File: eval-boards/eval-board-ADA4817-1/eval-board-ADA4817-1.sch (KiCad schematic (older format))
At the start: 27 parts, among them J2 -VIN, J3 +VIN, J4 Conn_01x03_Male, J5 VOUT, U1 ADA4817-1

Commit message: second-order_active_filter
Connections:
- net GNDREF: now also C10.1; no longer C10.2
- net VEE: now also C10.2; no longer C10.1
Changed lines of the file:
@@
 EESchema Schematic File Version 4
+LIBS:eval-board-ADA4817-1-cache
 EELAYER 29 0
 EELAYER END
@@
 F 3 "~" H 7400 4950 50  0001 C CNN
 	1    7400 4950
-	1    0    0    -1
-$EndComp
-$Comp
+	-1   0    0    1
+$EndComp
+$Comp

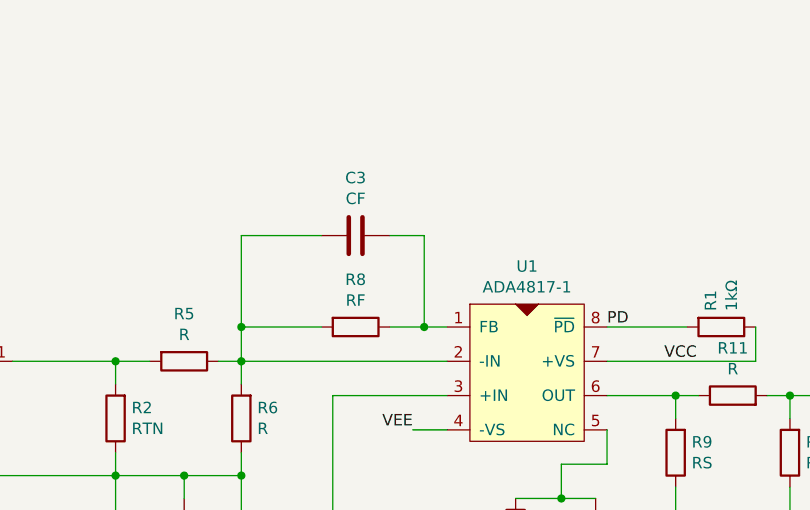
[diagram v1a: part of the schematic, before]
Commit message: power_and_RF_updated
修正了ADA4817和有源滤波器的电源线管脚、反馈电阻和焊盘handsold
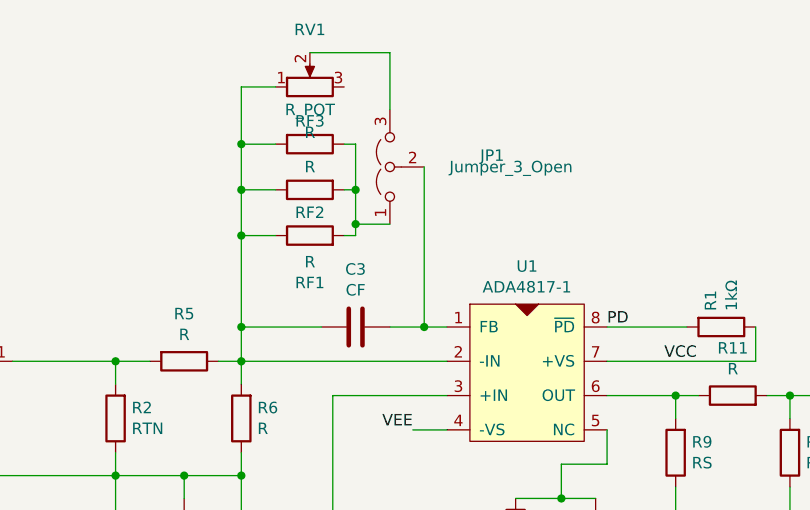
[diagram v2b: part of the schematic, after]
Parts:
- added JP1: Jumper_3_Open, Jumper:SolderJumper-3_P1.3mm_Open_RoundedPad1.0x1.5mm_NumberLabels, symbol Jumper:Jumper_3_Open
- added RF2, RF3: R, Resistor_SMD:R_0603_1608Metric_Pad1.05x0.95mm_HandSolder, symbol Device:R
- added RV1: R_POT, Connector_PinSocket_2.54mm:PinSocket_1x03_P2.54mm_Vertical, symbol Device:R_POT
- C1, C2, C3, C5, C6, C7, C8, C9: footprint Capacitor_SMD:C_0603_1608Metric -> Capacitor_SMD:C_0603_1608Metric_Pad1.05x0.95mm_HandSolder
- C10, C4: footprint Capacitor_SMD:CP_Elec_4x5.3 -> Capacitor_SMD:CP_Elec_4x5.4
- J4: footprint Connector_PinSocket_2.54mm:PinSocket_1x03_P2.54mm_Vertical -> Connector_JST:JST_XH_B3B-XH-A_1x03_P2.50mm_Vertical
- R1, R10, R11, R12, R2, R3, R4, R5, R6, R7, R9: footprint Resistor_SMD:R_0603_1608Metric -> Resistor_SMD:R_0603_1608Metric_Pad1.05x0.95mm_HandSolder
- RF1: renamed from R8; value RF -> R; footprint Resistor_SMD:R_0603_1608Metric -> Resistor_SMD:R_0603_1608Metric_Pad1.05x0.95mm_HandSolder
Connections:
- net at C3.1, U1.1 (FB): now also JP1.2 (C); no longer RF1.1
- net at C3.2, R5.1, R6.2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: now also RF1.1, RF2.1, RF3.2, RV1.1; no longer RF1.2
- new net: JP1.1 (A), RF1.2, RF2.2, RF3.1
- new net: JP1.3 (B), RV1.2
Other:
- moved on the sheet: C3, RF1
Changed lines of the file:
@@
 F 0 "R5" V 3843 2800 50  0000 C CNN
 F 1 "R" V 3934 2800 50  0000 C CNN
-F 2 "Resistor_SMD:R_0603_1608Metric" V 3980 2800 50  0001 C CNN
+F 2 "Resistor_SMD:R_0603_1608Metric_Pad1.05x0.95mm_HandSolder" V 3980 2800 50  0001 C CNN
 F 3 "~" H 4050 2800 50  0001 C CNN
 	1    4050 2800
@@
 F 0 "R6" H 4230 3004 50  0000 R CNN
 F 1 "R" H 4230 3095 50  0000 R CNN
-F 2 "Resistor_SMD:R_0603_1608Metric" V 4230 3050 50  0001 C CNN
+F 2 "Resistor_SMD:R_0603_1608Metric_Pad1.05x0.95mm_HandSolder" V 4230 3050 50  0001 C CNN
 F 3 "~" H 4300 3050 50  0001 C CNN
 	1    4300 3050
@@
 F 0 "R2" H 3680 3004 50  0000 R CNN
 F 1 "RTN" H 3680 3095 50  0000 R CNN
-F 2 "Resistor_SMD:R_0603_1608Metric" V 3680 3050 50  0001 C CNN
+F 2 "Resistor_SMD:R_0603_1608Metric_Pad1.05x0.95mm_HandSolder" V 3680 3050 50  0001 C CNN
 F 3 "~" H 3750 3050 50  0001 C CNN
 	1    3750 3050
@@
 	3100 3000 3100 3300
 Connection ~ 3750 3300
-$Comp
-L Device:R R8
-U 1 1 5D1F3FF1
+Wire Wire Line
+	4650 2650 4300 2650
+Wire Wire Line
+	4300 2650 4300 2800
+$Comp
+L Device:C C3
+U 1 1 5D1F4AF7
 P 4800 2650
-F 0 "R8" V 4593 2650 50  0000 C CNN
-F 1 "RF" V 4684 2650 50  0000 C CNN
-F 2 "Resistor_SMD:R_0603_1608Metric" V 4730 2650 50  0001 C CNN
+F 0 "C3" V 4548 2650 50  0000 C CNN
+F 1 "CF" V 4639 2650 50  0000 C CNN
+F 2 "Capacitor_SMD:C_0603_1608Metric_Pad1.05x0.95mm_HandSolder" H 4838 2500 50  0001 C CNN
 F 3 "~" H 4800 2650 50  0001 C CNN
 	1    4800 2650
@@
 $EndComp
 Wire Wire Line
-	4950 2650 5100 2650
-Wire Wire Line
-	4650 2650 4300 2650
-Wire Wire Line
-	4300 2650 4300 2800
-$Comp
-L Device:C C3
-U 1 1 5D1F4AF7
-P 4800 2250
-F 0 "C3" V 4548 2250 50  0000 C CNN
-F 1 "CF" V 4639 2250 50  0000 C CNN
-F 2 "Capacitor_SMD:C_0603_1608Metric" H 4838 2100 50  0001 C CNN
-F 3 "~" H 4800 2250 50  0001 C CNN
-	1    4800 2250
-	0    1    1    0
-$EndComp
-Wire Wire Line
-	4650 2250 4300 2250
-Wire Wire Line
 	4300 2250 4300 2650
 Connection ~ 4300 2650
-Wire Wire Line
-	4950 2250 5100 2250
-Wire Wire Line
-	5100 2250 5100 2650
-Connection ~ 5100 2650
-Wire Wire Line
-	5100 2650 5200 2650
 $Comp
 L Device:R R4
@@
 F 0 "R4" V 3793 4100 50  0000 C CNN
 F 1 "R" V 3884 4100 50  0000 C CNN
-F 2 "Resistor_SMD:R_0603_1608Metric" V 3930 4100 50  0001 C CNN
+F 2 "Resistor_SMD:R_0603_1608Metric_Pad1.05x0.95mm_HandSolder" V 3930 4100 50  0001 C CNN
 F 3 "~" H 4000 4100 50  0001 C CNN
 	1    4000 4100
@@
 F 0 "R3" H 3680 3754 50  0000 R CNN
 F 1 "RTP" H 3680 3845 50  0000 R CNN
-F 2 "Resistor_SMD:R_0603_1608Metric" V 3680 3800 50  0001 C CNN
+F 2 "Resistor_SMD:R_0603_1608Metric_Pad1.05x0.95mm_HandSolder" V 3680 3800 50  0001 C CNN
 F 3 "~" H 3750 3800 50  0001 C CNN
 	1    3750 3800
@@
 F 0 "R7" H 4230 3754 50  0000 R CNN
 F 1 "R" H 4230 3845 50  0000 R CNN
-F 2 "Resistor_SMD:R_0603_1608Metric" V 4230 3800 50  0001 C CNN
+F 2 "Resistor_SMD:R_0603_1608Metric_Pad1.05x0.95mm_HandSolder" V 4230 3800 50  0001 C CNN
 F 3 "~" H 4300 3800 50  0001 C CNN
 	1    4300 3800
@@
 F 0 "R9" H 6130 3154 50  0000 R CNN
 F 1 "RS" H 6130 3245 50  0000 R CNN
-F 2 "Resistor_SMD:R_0603_1608Metric" V 6130 3200 50  0001 C CNN
+F 2 "Resistor_SMD:R_0603_1608Metric_Pad1.05x0.95mm_HandSolder" V 6130 3200 50  0001 C CNN
 F 3 "~" H 6200 3200 50  0001 C CNN
 	1    6200 3200
@@
 F 0 "R11" V 6657 2950 50  0000 C CNN
 F 1 "R" V 6566 2950 50  0000 C CNN
-F 2 "Resistor_SMD:R_0603_1608Metric" V 6380 2950 50  0001 C CNN
+F 2 "Resistor_SMD:R_0603_1608Metric_Pad1.05x0.95mm_HandSolder" V 6380 2950 50  0001 C CNN
 F 3 "~" H 6450 2950 50  0001 C CNN
 	1    6450 2950
@@
 F 0 "R12" H 6630 3154 50  0000 R CNN
 F 1 "R" H 6630 3245 50  0000 R CNN
-F 2 "Resistor_SMD:R_0603_1608Metric" V 6630 3200 50  0001 C CNN
+F 2 "Resistor_SMD:R_0603_1608Metric_Pad1.05x0.95mm_HandSolder" V 6630 3200 50  0001 C CNN
 F 3 "~" H 6700 3200 50  0001 C CNN
 	1    6700 3200
@@
 F 0 "C5" H 6315 3696 50  0000 L CNN
 F 1 "CL" H 6315 3605 50  0000 L CNN
-F 2 "Capacitor_SMD:C_0603_1608Metric" H 6238 3500 50  0001 C CNN
+F 2 "Capacitor_SMD:C_0603_1608Metric_Pad1.05x0.95mm_HandSolder" H 6238 3500 50  0001 C CNN
 F 3 "~" H 6200 3650 50  0001 C CNN
 	1    6200 3650
@@
 F 0 "R10" V 5707 3550 50  0000 C CNN
 F 1 "R" V 5616 3550 50  0000 C CNN
-F 2 "Resistor_SMD:R_0603_1608Metric" V 5430 3550 50  0001 C CNN
+F 2 "Resistor_SMD:R_0603_1608Metric_Pad1.05x0.95mm_HandSolder" V 5430 3550 50  0001 C CNN
 F 3 "~" H 5500 3550 50  0001 C CNN
 	1    5500 3550
@@
 F 0 "C6" V 5598 3550 50  0000 C CNN
 F 1 "C" V 5689 3550 50  0000 C CNN
-F 2 "Capacitor_SMD:C_0603_1608Metric" H 5888 3400 50  0001 C CNN
+F 2 "Capacitor_SMD:C_0603_1608Metric_Pad1.05x0.95mm_HandSolder" H 5888 3400 50  0001 C CNN
 F 3 "~" H 5850 3550 50  0001 C CNN
 	1    5850 3550
@@
 F 0 "C8" V 5448 4000 50  0000 C CNN
 F 1 "C" V 5539 4000 50  0000 C CNN
-F 2 "Capacitor_SMD:C_0603_1608Metric" H 5738 3850 50  0001 C CNN
+F 2 "Capacitor_SMD:C_0603_1608Metric_Pad1.05x0.95mm_HandSolder" H 5738 3850 50  0001 C CNN
 F 3 "~" H 5700 4000 50  0001 C CNN
 	1    5700 4000
@@
 F 0 "R1" H 6330 2604 50  0000 R CNN
 F 1 "1kΩ" H 6330 2695 50  0000 R CNN
-F 2 "Resistor_SMD:R_0603_1608Metric" V 6330 2650 50  0001 C CNN
+F 2 "Resistor_SMD:R_0603_1608Metric_Pad1.05x0.95mm_HandSolder" V 6330 2650 50  0001 C CNN
 F 3 "~" H 6400 2650 50  0001 C CNN
 	1    6400 2650
@@
 F 0 "C10" H 7515 4996 50  0000 L CNN
 F 1 "10uF" H 7515 4905 50  0000 L CNN
-F 2 "Capacitor_SMD:CP_Elec_4x5.3" H 7400 4950 50  0001 C CNN
+F 2 "Capacitor_SMD:CP_Elec_4x5.4" H 7400 4950 50  0001 C CNN
 F 3 "~" H 7400 4950 50  0001 C CNN
 	1    7400 4950
@@
 F 0 "C4" H 4915 4946 50  0000 L CNN
 F 1 "10uF" H 4915 4855 50  0000 L CNN
-F 2 "Capacitor_SMD:CP_Elec_4x5.3" H 4800 4900 50  0001 C CNN
+F 2 "Capacitor_SMD:CP_Elec_4x5.4" H 4800 4900 50  0001 C CNN
 F 3 "~" H 4800 4900 50  0001 C CNN
 	1    4800 4900
@@
 F 0 "C1" H 4315 4946 50  0000 L CNN
 F 1 "0.1uF" H 4315 4855 50  0000 L CNN
-F 2 "Capacitor_SMD:C_0603_1608Metric" H 4238 4750 50  0001 C CNN
+F 2 "Capacitor_SMD:C_0603_1608Metric_Pad1.05x0.95mm_HandSolder" H 4238 4750 50  0001 C CNN
 F 3 "~" H 4200 4900 50  0001 C CNN
 	1    4200 4900
@@
 F 0 "C9" H 7215 4996 50  0000 L CNN
 F 1 "0.1uF" H 7215 4905 50  0000 L CNN
-F 2 "Capacitor_SMD:C_0603_1608Metric" H 7138 4800 50  0001 C CNN
+F 2 "Capacitor_SMD:C_0603_1608Metric_Pad1.05x0.95mm_HandSolder" H 7138 4800 50  0001 C CNN
 F 3 "~" H 7100 4950 50  0001 C CNN
 	1    7100 4950
@@
 F 0 "C7" H 6815 4996 50  0000 L CNN
 F 1 "0.1uF" H 6815 4905 50  0000 L CNN
-F 2 "Capacitor_SMD:C_0603_1608Metric" H 6738 4800 50  0001 C CNN
+F 2 "Capacitor_SMD:C_0603_1608Metric_Pad1.05x0.95mm_HandSolder" H 6738 4800 50  0001 C CNN
 F 3 "~" H 6700 4950 50  0001 C CNN
 	1    6700 4950
@@
 F 0 "C2" H 4665 4946 50  0000 L CNN
 F 1 "0.1uF" H 4665 4855 50  0000 L CNN
-F 2 "Capacitor_SMD:C_0603_1608Metric" H 4588 4750 50  0001 C CNN
+F 2 "Capacitor_SMD:C_0603_1608Metric_Pad1.05x0.95mm_HandSolder" H 4588 4750 50  0001 C CNN
 F 3 "~" H 4550 4900 50  0001 C CNN
 	1    4550 4900
@@
 F 0 "J4" V 5512 4694 50  0000 L CNN
 F 1 "Conn_01x03_Male" V 5603 4694 50  0000 L CNN
-F 2 "Connector_PinSocket_2.54mm:PinSocket_1x03_P2.54mm_Vertical" H 5450 4550 50  0001 C CNN
+F 2 "Connector_JST:JST_XH_B3B-XH-A_1x03_P2.50mm_Vertical" H 5450 4550 50  0001 C CNN
 F 3 "~" H 5450 4550 50  0001 C CNN
 	1    5450 4550
@@
 Wire Wire Line
 	5200 3100 5050 3100
+$Comp
+L Device:R RF2
+U 1 1 5D22C675
+P 4600 2050
+F 0 "RF2" V 4700 2050 50  0000 C CNN
+F 1 "R" V 4500 2050 50  0000 C CNN
+F 2 "Resistor_SMD:R_0603_1608Metric_Pad1.05x0.95mm_HandSolder" V 4530 2050 50  0001 C CNN
+F 3 "~" H 4600 2050 50  0001 C CNN
+	1    4600 2050
+	0    -1   1    0
+$EndComp
+$Comp
+L Device:R_POT RV1
+U 1 1 5D22DEC7
+P 4600 1600
+F 0 "RV1" V 4850 1600 50  0000 C CNN
+F 1 "R_POT" V 4500 1600 50  0000 C CNN
+F 2 "Connector_PinSocket_2.54mm:PinSocket_1x03_P2.54mm_Vertical" H 4600 1600 50  0001 C CNN
+F 3 "~" H 4600 1600 50  0001 C CNN
+	1    4600 1600
+	0    -1   -1   0
+$EndComp
+Wire Wire Line
+	4950 2650 5100 2650
+Wire Wire Line
+	4450 2250 4300 2250
+Wire Wire Line
+	4450 1850 4300 1850
+Wire Wire Line
+	4300 1850 4300 2050
+Connection ~ 4300 2250
+Wire Wire Line
+	4450 2050 4300 2050
+Connection ~ 4300 2050
+Wire Wire Line
+	4300 2050 4300 2250
+Wire Wire Line
+	4450 1600 4300 1600
+Wire Wire Line
+	4300 1600 4300 1850
+Connection ~ 4300 1850
+$Comp
+L Jumper:Jumper_3_Open JP1
+U 1 1 5D243A9D
+P 4950 1950
+F 0 "JP1" V 5000 1450 50  0000 L CNN
+F 1 "Jumper_3_Open" V 4950 1150 50  0000 L CNN
+F 2 "Jumper:SolderJumper-3_P1.3mm_Open_RoundedPad1.0x1.5mm_NumberLabels" H 4950 1950 50  0001 C CNN
+F 3 "~" H 4950 1950 50  0001 C CNN
+	1    4950 1950
+	0    -1   -1   0
+$EndComp
+Wire Wire Line
+	5100 1950 5100 2650
+Connection ~ 5100 2650
+Wire Wire Line
+	5100 2650 5200 2650
+Wire Wire Line
+	4950 1700 4950 1450
+Wire Wire Line
+	4950 1450 4600 1450
+Wire Wire Line
+	4950 2200 4800 2200
+Wire Wire Line
+	4800 2200 4800 2250
+Wire Wire Line
+	4800 2250 4750 2250
+Wire Wire Line
+	4750 2050 4800 2050
+Wire Wire Line
+	4800 2050 4800 2200
+Connection ~ 4800 2200
+Wire Wire Line
+	4750 1850 4800 1850
+Wire Wire Line
+	4800 1850 4800 2050
+Connection ~ 4800 2050
+$Comp
+L Device:R RF1
+U 1 1 5D1F3FF1
+P 4600 2250
+F 0 "RF1" V 4393 2250 50  0000 C CNN
+F 1 "R" V 4484 2250 50  0000 C CNN
+F 2 "Resistor_SMD:R_0603_1608Metric_Pad1.05x0.95mm_HandSolder" V 4530 2250 50  0001 C CNN
+F 3 "~" H 4600 2250 50  0001 C CNN
+	1    4600 2250
+	0    -1   -1   0
+$EndComp
+$Comp
+L Device:R RF3
+U 1 1 5D2342B5
+P 4600 1850
+F 0 "RF3" V 4500 1850 50  0000 C CNN
+F 1 "R" V 4550 1850 50  0000 C CNN
+F 2 "Resistor_SMD:R_0603_1608Metric_Pad1.05x0.95mm_HandSolder" V 4530 1850 50  0001 C CNN
+F 3 "~" H 4600 1850 50  0001 C CNN
+	1    4600 1850
+	0    1    1    0
+$EndComp
 $EndSCHEMATC
